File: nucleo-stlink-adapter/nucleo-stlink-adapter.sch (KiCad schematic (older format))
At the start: 4 parts, among them J1 Conn_02x05_Odd_Even, J2 Conn_01x06_Female, SW1 RESET

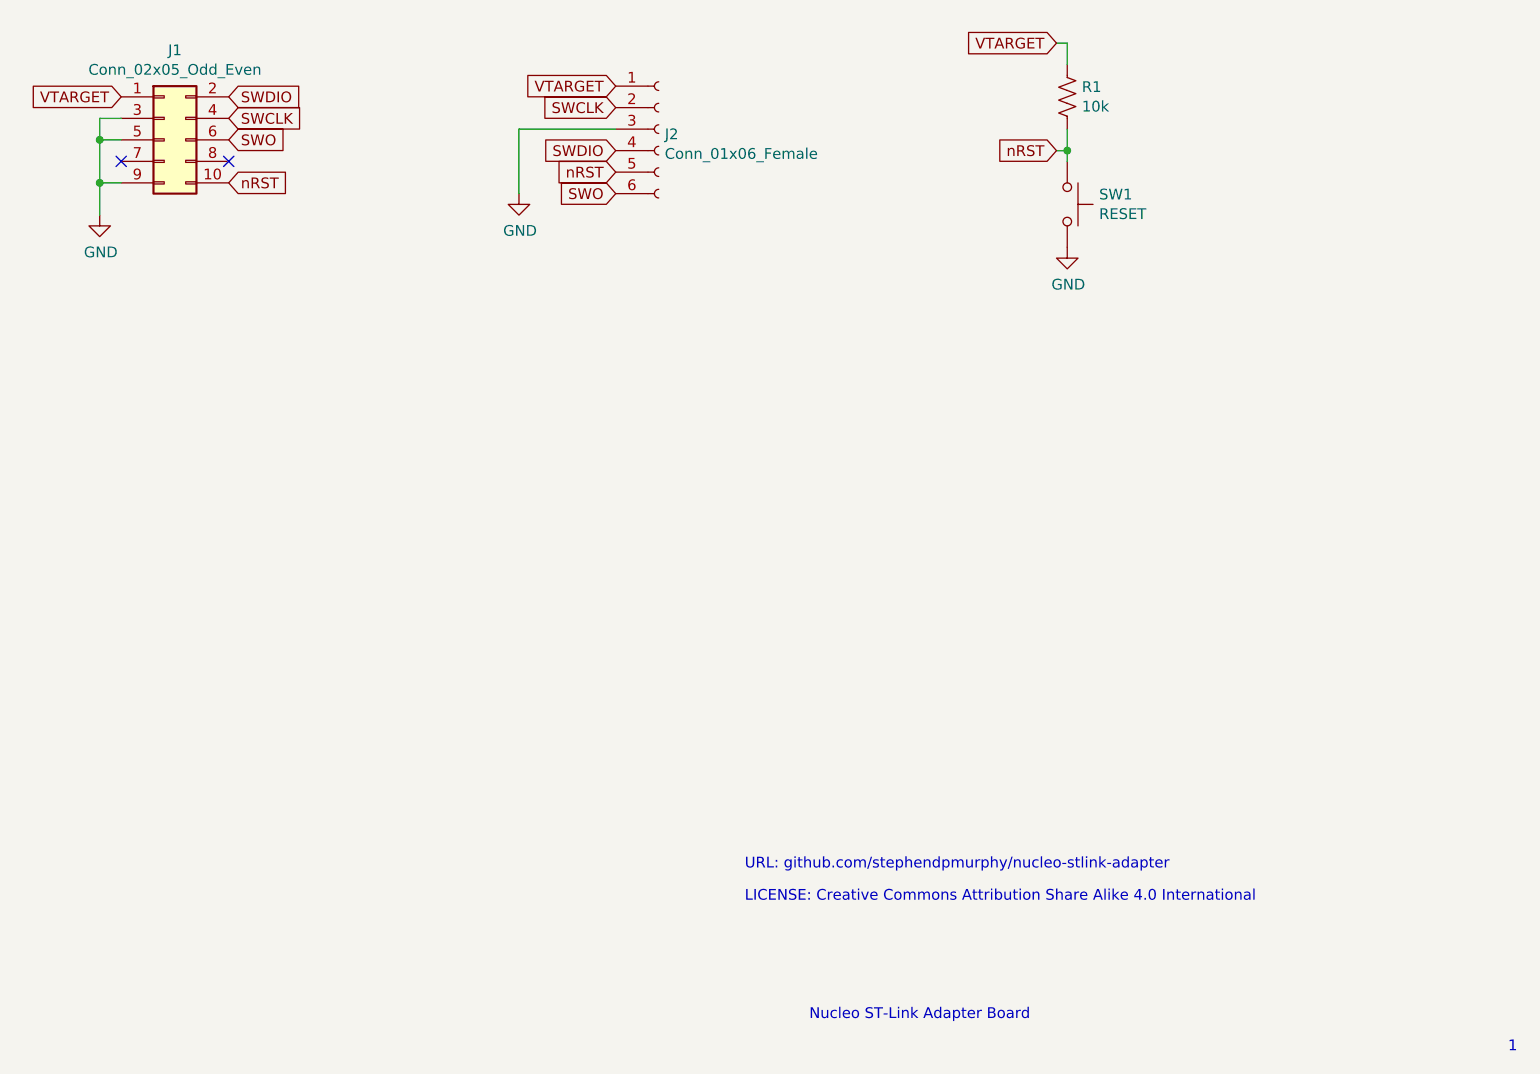
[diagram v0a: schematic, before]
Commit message: Cleaned up schematic and board
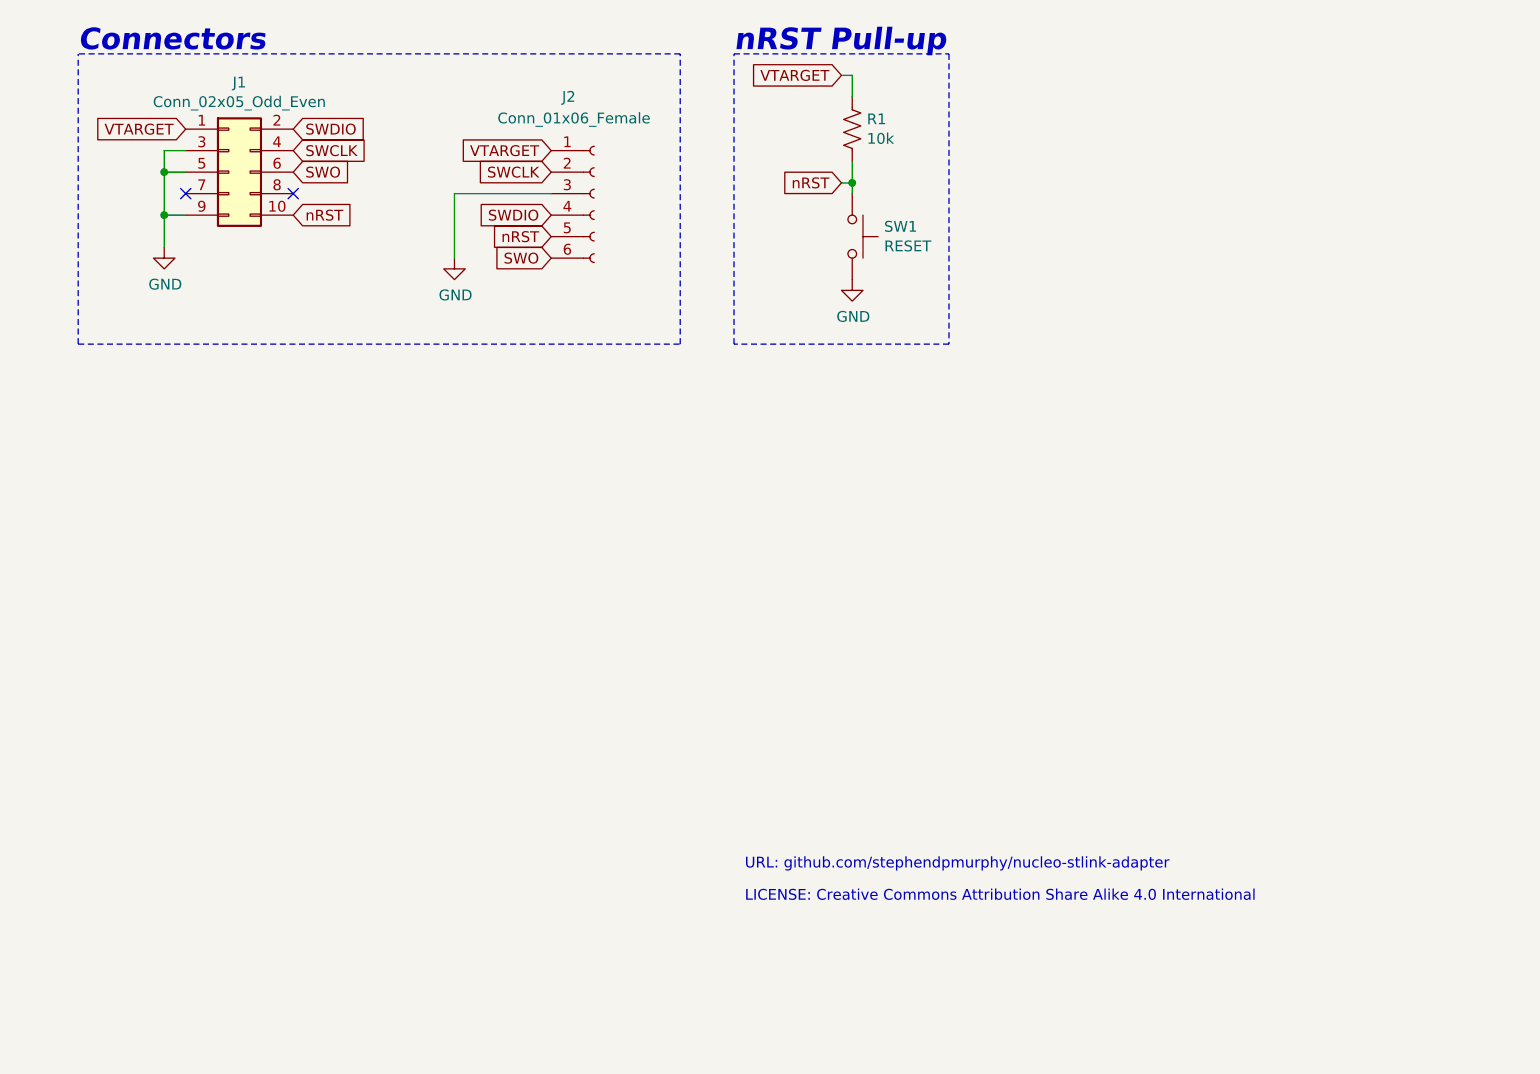
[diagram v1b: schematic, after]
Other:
- note added: "Connectors"
- note added: "nRST Pull-up"
- note removed: "1"
- note removed: "Nucleo ST-Link Adapter Board"
- moved on the sheet: J1, J2, R1, SW1
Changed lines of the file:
@@
 encoding utf-8
 Sheet 1 1
-Title ""
-Date ""
-Rev ""
+Title "nucleo-stlink-adapter"
+Date "2020-08-21"
+Rev "1"
 Comp ""
 Comment1 ""
@@
 L Connector:Conn_01x06_Female J2
 U 1 1 5F1F751D
-P 6650 3350
-F 0 "J2" H 6678 3326 50  0000 L CNN
-F 1 "Conn_01x06_Female" H 6678 3235 50  0000 L CNN
-F 2 "Connector_PinHeader_2.54mm:PinHeader_1x06_P2.54mm_Vertical" H 6650 3350 50  0001 C CNN
-F 3 "~" H 6650 3350 50  0001 C CNN
-	1    6650 3350
+P 6350 3650
+F 0 "J2" H 6200 4100 50  0000 L CNN
+F 1 "Conn_01x06_Female" H 5900 4000 50  0000 L CNN
+F 2 "Connector_PinHeader_2.54mm:PinHeader_1x06_P2.54mm_Vertical" H 6350 3650 50  0001 C CNN
+F 3 "~" H 6350 3650 50  0001 C CNN
+	1    6350 3650
 	1    0    0    -1
 $EndComp
@@
 L Connector_Generic:Conn_02x05_Odd_Even J1
 U 1 1 5F1F8AEA
-P 4350 3400
-F 0 "J1" H 4400 3817 50  0000 C CNN
-F 1 "Conn_02x05_Odd_Even" H 4400 3726 50  0000 C CNN
-F 2 "Connector_PinHeader_1.27mm:PinHeader_2x05_P1.27mm_Vertical_SMD" H 4350 3400 50  0001 C CNN
-F 3 "~" H 4350 3400 50  0001 C CNN
-	1    4350 3400
+P 4650 3550
+F 0 "J1" H 4700 3967 50  0000 C CNN
+F 1 "Conn_02x05_Odd_Even" H 4700 3876 50  0000 C CNN
+F 2 "Connector_PinHeader_1.27mm:PinHeader_2x05_P1.27mm_Vertical_SMD" H 4650 3550 50  0001 C CNN
+F 3 "~" H 4650 3550 50  0001 C CNN
+	1    4650 3550
 	1    0    0    -1
 $EndComp
@@
 L Device:R_US R1
 U 1 1 5F1FA6DA
-P 8550 3200
-F 0 "R1" H 8482 3154 50  0000 R CNN
-F 1 "10k" H 8482 3245 50  0000 R CNN
-F 2 "Resistor_SMD:R_0603_1608Metric" V 8590 3190 50  0001 C CNN
-F 3 "~" H 8550 3200 50  0001 C CNN
-	1    8550 3200
+P 7550 3350
+F 0 "R1" H 7482 3304 50  0000 R CNN
+F 1 "10k" H 7482 3395 50  0000 R CNN
+F 2 "Resistor_SMD:R_0603_1608Metric" V 7590 3340 50  0001 C CNN
+F 3 "~" H 7550 3350 50  0001 C CNN
+	1    7550 3350
 	-1   0    0    1
 $EndComp
@@
 L power:GND #PWR0101
 U 1 1 5F1FBF32
-P 8550 3900
-F 0 "#PWR0101" H 8550 3650 50  0001 C CNN
-F 1 "GND" H 8555 3727 50  0000 C CNN
-F 2 "" H 8550 3900 50  0001 C CNN
-F 3 "" H 8550 3900 50  0001 C CNN
-	1    8550 3900
+P 7550 4050
+F 0 "#PWR0101" H 7550 3800 50  0001 C CNN
+F 1 "GND" H 7555 3877 50  0000 C CNN
+F 2 "" H 7550 4050 50  0001 C CNN
+F 3 "" H 7550 4050 50  0001 C CNN
+	1    7550 4050
 	1    0    0    -1
 $EndComp
-Text GLabel 4650 3200 2    50   Input ~ 0
+Text GLabel 4950 3350 2    50   Input ~ 0
 SWDIO
-Text GLabel 4650 3300 2    50   Input ~ 0
+Text GLabel 4950 3450 2    50   Input ~ 0
 SWCLK
-Text GLabel 4650 3600 2    50   Input ~ 0
+Text GLabel 4950 3750 2    50   Input ~ 0
 nRST
-Text GLabel 4150 3200 0    50   Input ~ 0
+Text GLabel 4450 3350 0    50   Input ~ 0
 VTARGET
-NoConn ~ 4150 3500
-NoConn ~ 4650 3500
-Text GLabel 6450 3150 0    50   Input ~ 0
+NoConn ~ 4450 3650
+NoConn ~ 4950 3650
+Text GLabel 6150 3450 0    50   Input ~ 0
 VTARGET
-Text GLabel 6450 3250 0    50   Input ~ 0
+Text GLabel 6150 3550 0    50   Input ~ 0
 SWCLK
-Text GLabel 6450 3450 0    50   Input ~ 0
+Text GLabel 6150 3750 0    50   Input ~ 0
 SWDIO
-Text GLabel 6450 3550 0    50   Input ~ 0
+Text GLabel 6150 3850 0    50   Input ~ 0
 nRST
 $Comp
 L power:GND #PWR0102
 U 1 1 5F1FFBE8
-P 6000 3650
-F 0 "#PWR0102" H 6000 3400 50  0001 C CNN
-F 1 "GND" H 6005 3477 50  0000 C CNN
-F 2 "" H 6000 3650 50  0001 C CNN
-F 3 "" H 6000 3650 50  0001 C CNN
-	1    6000 3650
+P 5700 3950
+F 0 "#PWR0102" H 5700 3700 50  0001 C CNN
+F 1 "GND" H 5705 3777 50  0000 C CNN
+F 2 "" H 5700 3950 50  0001 C CNN
+F 3 "" H 5700 3950 50  0001 C CNN
+	1    5700 3950
 	1    0    0    -1
 $EndComp
@@
 L power:GND #PWR0103
 U 1 1 5F1FE333
-P 4050 3750
-F 0 "#PWR0103" H 4050 3500 50  0001 C CNN
-F 1 "GND" H 4055 3577 50  0000 C CNN
-F 2 "" H 4050 3750 50  0001 C CNN
-F 3 "" H 4050 3750 50  0001 C CNN
-	1    4050 3750
+P 4350 3900
+F 0 "#PWR0103" H 4350 3650 50  0001 C CNN
+F 1 "GND" H 4355 3727 50  0000 C CNN
+F 2 "" H 4350 3900 50  0001 C CNN
+F 3 "" H 4350 3900 50  0001 C CNN
+	1    4350 3900
 	1    0    0    -1
 $EndComp
 Wire Wire Line
-	4150 3600 4050 3600
+	4450 3750 4350 3750
 Wire Wire Line
-	4050 3600 4050 3750
+	4350 3750 4350 3900
 Wire Wire Line
-	4150 3400 4050 3400
+	4450 3550 4350 3550
 Wire Wire Line
-	4050 3400 4050 3600
-Connection ~ 4050 3600
+	4350 3550 4350 3750
+Connection ~ 4350 3750
 Wire Wire Line
-	4150 3300 4050 3300
+	4450 3450 4350 3450
 Wire Wire Line
-	4050 3300 4050 3400
-Connection ~ 4050 3400
-Text GLabel 8500 2950 0    50   Input ~ 0
+	4350 3450 4350 3550
+Connection ~ 4350 3550
+Text GLabel 7500 3100 0    50   Input ~ 0
 VTARGET
 Wire Wire Line
-	8500 2950 8550 2950
+	7500 3100 7550 3100
 Wire Wire Line
-	8550 2950 8550 3050
+	7550 3100 7550 3200
 Wire Wire Line
-	8550 3500 8550 3450
-Text GLabel 8500 3450 0    50   Input ~ 0
+	7550 3650 7550 3600
+Text GLabel 7500 3600 0    50   Input ~ 0
 nRST
 Wire Wire Line
-	8500 3450 8550 3450
-Connection ~ 8550 3450
+	7500 3600 7550 3600
+Connection ~ 7550 3600
 Wire Wire Line
-	8550 3450 8550 3350
+	7550 3600 7550 3500
 Text Notes 7050 6800 0    50   ~ 0
 URL: github.com/stephendpmurphy/nucleo-stlink-adapter
 Text Notes 7050 6950 0    50   ~ 0
 LICENSE: Creative Commons Attribution Share Alike 4.0 International
-Text Notes 7350 7500 0    50   ~ 0
-Nucleo ST-Link Adapter Board
-Text Notes 10600 7650 0    50   ~ 0
-1
 Wire Wire Line
-	6450 3350 6000 3350
+	6150 3650 5700 3650
 Wire Wire Line
-	6000 3350 6000 3650
+	5700 3650 5700 3950
 $Comp
 L Switch:SW_Push SW1
 U 1 1 5F1F9419
-P 8550 3700
-F 0 "SW1" V 8504 3848 50  0000 L CNN
-F 1 "RESET" V 8595 3848 50  0000 L CNN
-F 2 "Button_Switch_SMD:SW_SPST_TL3342" H 8550 3900 50  0001 C CNN
-F 3 "~" H 8550 3900 50  0001 C CNN
-	1    8550 3700
+P 7550 3850
+F 0 "SW1" V 7504 3998 50  0000 L CNN
+F 1 "RESET" V 7595 3998 50  0000 L CNN
+F 2 "Button_Switch_SMD:SW_SPST_TL3342" H 7550 4050 50  0001 C CNN
+F 3 "~" H 7550 4050 50  0001 C CNN
+	1    7550 3850
 	0    1    1    0
 $EndComp
-Text GLabel 4650 3400 2    50   Input ~ 0
+Text GLabel 4950 3550 2    50   Input ~ 0
 SWO
-Text GLabel 6450 3650 0    50   Input ~ 0
+Text GLabel 6150 3950 0    50   Input ~ 0
 SWO
+Wire Notes Line
+	3950 4350 3950 3000
+Wire Notes Line
+	7000 3000 8000 3000
+Wire Notes Line
+	8000 3000 8000 4350
+Wire Notes Line
+	8000 4350 7000 4350
+Wire Notes Line
+	7000 4350 7000 3000
+Text Notes 3950 3000 0    100  Italic 20
+Connectors
+Text Notes 7000 3000 0    100  Italic 20
+nRST Pull-up
+Wire Notes Line
+	3950 4350 6750 4350
+Wire Notes Line
+	6750 4350 6750 3000
+Wire Notes Line
+	6750 3000 3950 3000
 $EndSCHEMATC
